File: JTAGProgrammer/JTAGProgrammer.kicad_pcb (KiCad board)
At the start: 4 copper layers, 39 x 59 mm, 111 parts, among them J1 USB_B_Micro, J2 878325623, J3 Conn_01x06, J4 Conn_01x06, J5 Conn_01x03, U1 LP2985-3.3, U2 FT2232HL, U3 93LC56B, U4 74LVC3G17, U5 74LVC3G17, U6 74LVC3G17, U7 74LVC3G17, U8 LP2985-2.5, Y1 RH100-12.000-10-3030-TR

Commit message: Add LCSC part numbers
Signed-off-by: Anthony Bernaert <anthony.bernaert@gmail.com>
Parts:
- R6: value 12K 1% -> 12K
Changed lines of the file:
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@@
     (descr "SOD-323")
     (tags "SOD-323")
+    (property "LCSC" "C324473")
     (property "Sheetfile" "JTAG.kicad_sch")
     (property "Sheetname" "JTAG")
@@
   (footprint "PGB1010603MR:DIOC1608X36N" (layer "F.Cu")
     (at 98.5 85.349455 90)
+    (property "LCSC" "C142698")
     (property "MANUFACTURER" "Littelfuse Inc.")
     (property "MAXIMUM_PACKAGE_HEIGHT" "0.36 mm")
@@
     (descr "SOD-323")
     (tags "SOD-323")
+    (property "LCSC" "C324473")
     (property "Sheetfile" "JTAG.kicad_sch")
     (property "Sheetname" "JTAG")
@@
   (footprint "PGB1010603MR:DIOC1608X36N" (layer "F.Cu")
     (at 88.3 86 90)
+    (property "LCSC" "C142698")
     (property "MANUFACTURER" "Littelfuse Inc.")
     (property "MAXIMUM_PACKAGE_HEIGHT" "0.36 mm")
@@
   (footprint "PGB1010603MR:DIOC1608X36N" (layer "F.Cu")
     (at 101.9 84.4 180)
+    (property "LCSC" "C142698")
     (property "MANUFACTURER" "Littelfuse Inc.")
     (property "MAXIMUM_PACKAGE_HEIGHT" "0.36 mm")
@@
     (descr "SOT, 6 Pin (https://www.jedec.org/sites/default/files/docs/Mo-178c.PDF variant AB), generated with kicad-footprint-generator ipc_gullwing_generator.py")
     (tags "SOT TO_SOT_SMD")
+    (property "LCSC" "C190271")
     (property "Sheetfile" "FTDI.kicad_sch")
     (property "Sheetname" "FTDI")
@@
     (descr "Through hole straight socket strip, 1x06, 2.54mm pitch, single row (from Kicad 4.0.7), script generated")
     (tags "Through hole socket strip THT 1x06 2.54mm single row")
+    (property "LCSC" "C40877")
     (property "Sheetfile" "JTAG.kicad_sch")
     (property "Sheetname" "JTAG")
@@
         (effects (font (size 0.9 0.8) (thickness 0.15)))
     )
-    (fp_text value "12K 1%" (at 0.1 0.85) (layer "F.Fab")
+    (fp_text value "12K" (at 0.1 0.85) (layer "F.Fab")
         (effects (font (size 0.5 0.5) (thickness 0.15)))
     )
@@
     (descr "VSSOP-8 3.0 x 3.0, http://www.ti.com/lit/ds/symlink/lm75b.pdf")
     (tags "VSSOP-8 3.0 x 3.0")
+    (property "LCSC" "C18213")
     (property "Sheetfile" "UART.kicad_sch")
     (property "Sheetname" "UART")
@@
     (descr "Inductor SMD 0603 (1608 Metric), square (rectangular) end terminal, IPC_7351 nominal, (Body size source: http://www.tortai-tech.com/upload/download/2011102023233369053.pdf), generated with kicad-footprint-generator")
     (tags "inductor")
+    (property "LCSC" "C107335")
     (property "Sheetfile" "Power.kicad_sch")
     (property "Sheetname" "Power")
@@
     (descr "SMD Crystal SERIES SMD3225/4 http://www.txccrystal.com/images/pdf/7m-accuracy.pdf, 3.2x2.5mm^2 package")
     (tags "SMD SMT crystal")
+    (property "LCSC" "C255903")
     (property "Sheetfile" "FTDI.kicad_sch")
     (property "Sheetname" "FTDI")
@@
     (descr "VSSOP-8 3.0 x 3.0, http://www.ti.com/lit/ds/symlink/lm75b.pdf")
     (tags "VSSOP-8 3.0 x 3.0")
+    (property "LCSC" "C18213")
     (property "Sheetfile" "UART.kicad_sch")
     (property "Sheetname" "UART")
@@
     (descr "Inductor SMD 0603 (1608 Metric), square (rectangular) end terminal, IPC_7351 nominal, (Body size source: http://www.tortai-tech.com/upload/download/2011102023233369053.pdf), generated with kicad-footprint-generator")
     (tags "inductor")
+    (property "LCSC" "C107335")
     (property "Sheetfile" "Power.kicad_sch")
     (property "Sheetname" "Power")
@@
     (descr "Through hole straight socket strip, 1x03, 2.54mm pitch, single row (from Kicad 4.0.7), script generated")
     (tags "Through hole socket strip THT 1x03 2.54mm single row")
+    (property "LCSC" "C146243")
     (property "Sheetfile" "JTAGProgrammer.kicad_sch")
     (property "Sheetname" "")
@@
   (footprint "PGB1010603MR:DIOC1608X36N" (layer "F.Cu")
     (at 101.9 82.75 180)
+    (property "LCSC" "C142698")
     (property "MANUFACTURER" "Littelfuse Inc.")
     (property "MAXIMUM_PACKAGE_HEIGHT" "0.36 mm")
@@
   (footprint "PGB1010603MR:DIOC1608X36N" (layer "F.Cu")
     (at 91.3 48.4)
+    (property "LCSC" "C142698")
     (property "MANUFACTURER" "Littelfuse Inc.")
     (property "MAXIMUM_PACKAGE_HEIGHT" "0.36 mm")
@@
     (descr "VSSOP-8 3.0 x 3.0, http://www.ti.com/lit/ds/symlink/lm75b.pdf")
     (tags "VSSOP-8 3.0 x 3.0")
+    (property "LCSC" "C18213")
     (property "Sheetfile" "JTAG.kicad_sch")
     (property "Sheetname" "JTAG")
@@
     (descr "Through hole straight socket strip, 1x06, 2.54mm pitch, single row (from Kicad 4.0.7), script generated")
     (tags "Through hole socket strip THT 1x06 2.54mm single row")
+    (property "LCSC" "C40877")
     (property "Sheetfile" "UART.kicad_sch")
     (property "Sheetname" "UART")
@@
     (descr "VSSOP-8 3.0 x 3.0, http://www.ti.com/lit/ds/symlink/lm75b.pdf")
     (tags "VSSOP-8 3.0 x 3.0")
+    (property "LCSC" "C18213")
     (property "Sheetfile" "JTAG.kicad_sch")
     (property "Sheetname" "JTAG")
@@
   (footprint "PGB1010603MR:DIOC1608X36N" (layer "F.Cu")
     (at 92.45 86 90)
+    (property "LCSC" "C142698")
     (property "MANUFACTURER" "Littelfuse Inc.")
     (property "MAXIMUM_PACKAGE_HEIGHT" "0.36 mm")
@@
   (footprint "PGB1010603MR:DIOC1608X36N" (layer "F.Cu")
     (at 101.9 87.7 180)
+    (property "LCSC" "C142698")
     (property "MANUFACTURER" "Littelfuse Inc.")
     (property "MAXIMUM_PACKAGE_HEIGHT" "0.36 mm")
@@
     (descr "LQFP, 64 Pin (https://www.analog.com/media/en/technical-documentation/data-sheets/ad7606_7606-6_7606-4.pdf), generated with kicad-footprint-generator ipc_gullwing_generator.py")
     (tags "LQFP QFP")
+    (property "LCSC" "C27882")
     (property "Sheetfile" "FTDI.kicad_sch")
     (property "Sheetname" "FTDI")
@@
     (descr "SOD-323")
     (tags "SOD-323")
+    (property "LCSC" "C324473")
     (property "Sheetfile" "JTAG.kicad_sch")
     (property "Sheetname" "JTAG")
@@
     (descr "SOD-323")
     (tags "SOD-323")
+    (property "LCSC" "C324473")
     (property "Sheetfile" "UART.kicad_sch")
     (property "Sheetname" "UART")
@@
   (footprint "PGB1010603MR:DIOC1608X36N" (layer "F.Cu")
     (at 94.5 86.050545 90)
+    (property "LCSC" "C142698")
     (property "MANUFACTURER" "Littelfuse Inc.")
     (property "MAXIMUM_PACKAGE_HEIGHT" "0.36 mm")
@@
     (descr "USB Micro-B receptacle, horizontal, SMD, 10118194, https://cdn.amphenol-icc.com/media/wysiwyg/files/drawing/10118194.pdf")
     (tags "USB Micro B horizontal SMD")
+    (property "LCSC" "C132563")
     (property "Sheetfile" "JTAGProgrammer.kicad_sch")
     (property "Sheetname" "")
@@
   (footprint "PGB1010603MR:DIOC1608X36N" (layer "F.Cu")
     (at 90.45 86 90)
+    (property "LCSC" "C142698")
     (property "MANUFACTURER" "Littelfuse Inc.")
     (property "MAXIMUM_PACKAGE_HEIGHT" "0.36 mm")
@@
     (descr "SOD-323")
     (tags "SOD-323")
+    (property "LCSC" "C324473")
     (property "Sheetfile" "UART.kicad_sch")
     (property "Sheetname" "UART")
@@
   (footprint "PGB1010603MR:DIOC1608X36N" (layer "F.Cu")
     (at 88.25 48.4 180)
+    (property "LCSC" "C142698")
     (property "MANUFACTURER" "Littelfuse Inc.")
     (property "MAXIMUM_PACKAGE_HEIGHT" "0.36 mm")
@@
     (at 93.35 93)
     (tags "878325623 ")
+    (property "LCSC" "C5197958")
     (property "Sheetfile" "JTAG.kicad_sch")
     (property "Sheetname" "JTAG")
@@
   (footprint "PGB1010603MR:DIOC1608X36N" (layer "F.Cu")
     (at 101.95 81.099455 180)
+    (property "LCSC" "C142698")
     (property "MANUFACTURER" "Littelfuse Inc.")
     (property "MAXIMUM_PACKAGE_HEIGHT" "0.36 mm")
@@
     (descr "Inductor SMD 0603 (1608 Metric), square (rectangular) end terminal, IPC_7351 nominal, (Body size source: http://www.tortai-tech.com/upload/download/2011102023233369053.pdf), generated with kicad-footprint-generator")
     (tags "inductor")
+    (property "LCSC" "C107335")
     (property "Sheetfile" "Power.kicad_sch")
     (property "Sheetname" "Power")
@@
     (descr "SOD-323")
     (tags "SOD-323")
+    (property "LCSC" "C324473")
     (property "Sheetfile" "UART.kicad_sch")
     (property "Sheetname" "UART")

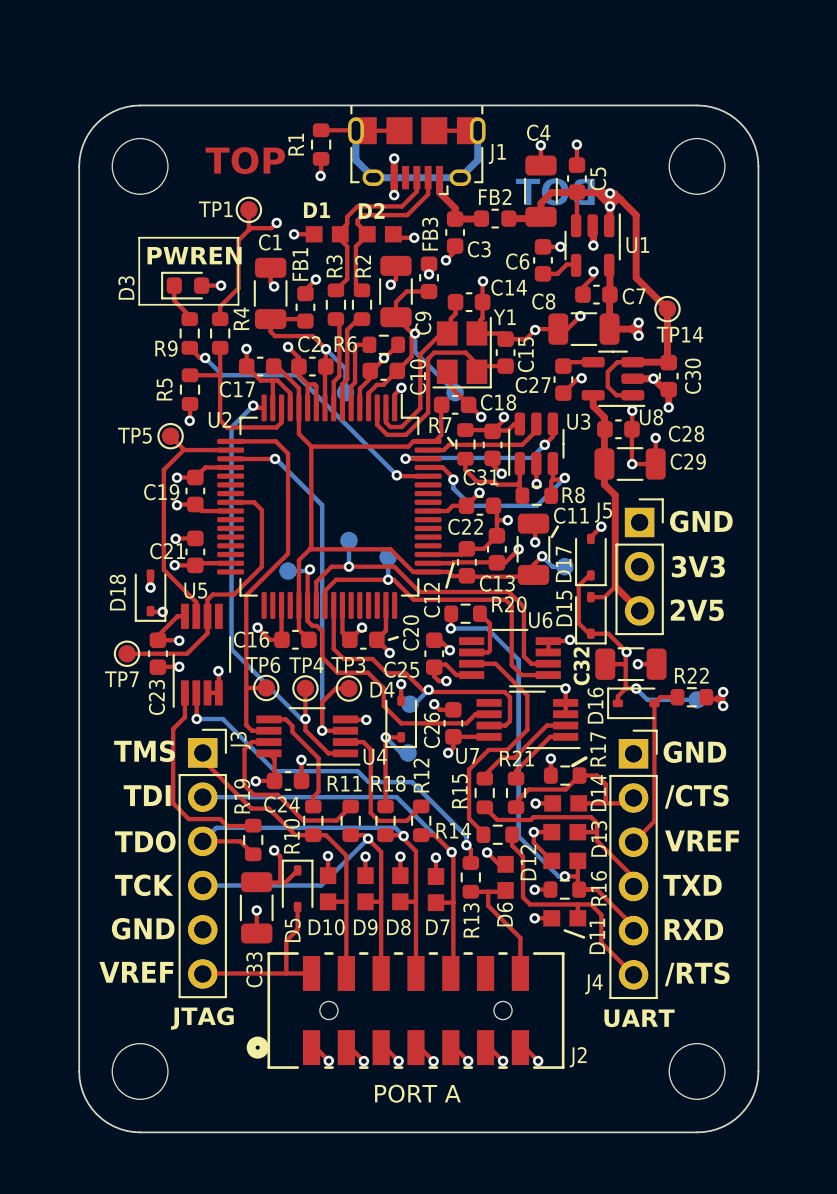
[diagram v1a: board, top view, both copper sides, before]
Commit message: Rev.2: change to USB Type-C, add VBUS fuse, VREF LED indicators
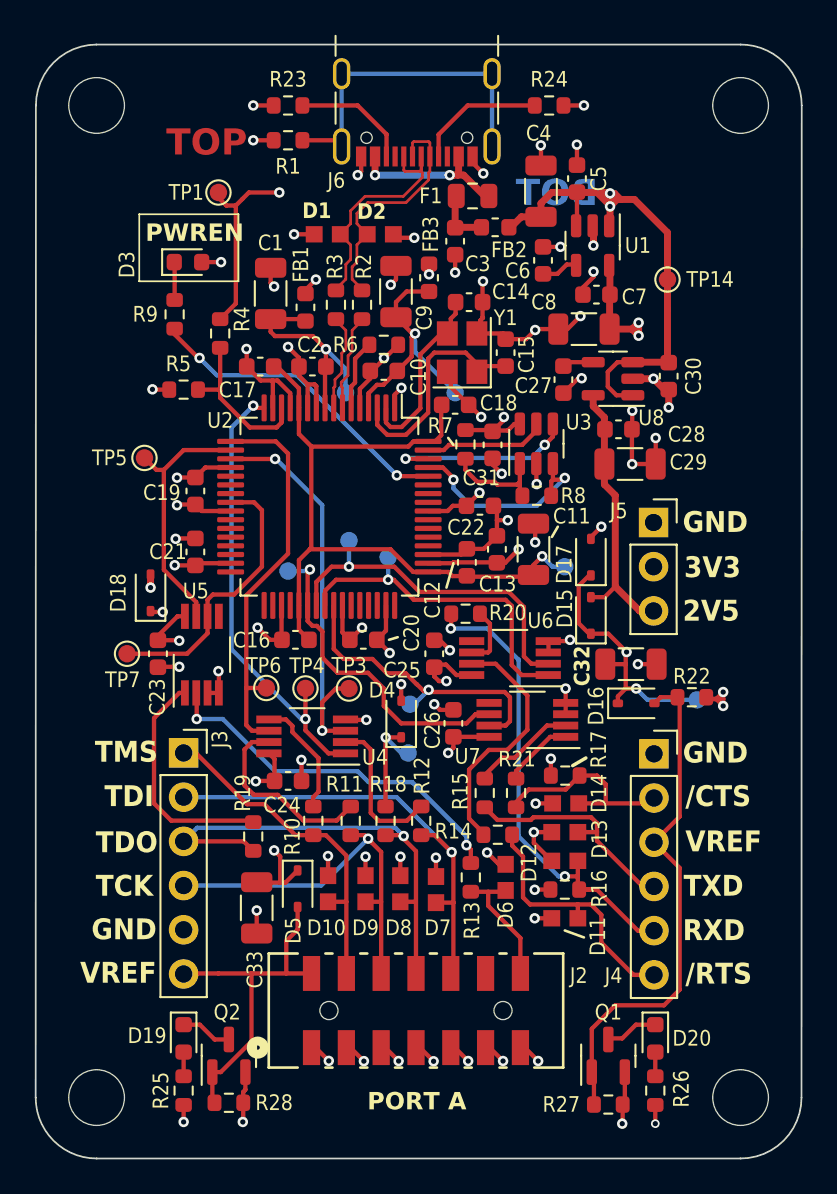
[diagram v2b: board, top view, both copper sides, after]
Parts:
- removed J1: USB_B_Micro, Connector_USB:USB_Micro-B_Amphenol_10118194_Horizontal
- added D19: LED, LED_SMD:LED_0603_1608Metric, F.Cu at (80.0, 94.6)
- added D20: LED, LED_SMD:LED_0603_1608Metric, F.Cu at (107.1, 94.6)
- added F1: 0805L075SLYR, Fuse:Fuse_0805_2012Metric, F.Cu at (96.6, 46.2)
- added J6: USB_C_Receptacle_USB2.0, Connector_USB:USB_C_Receptacle_GCT_USB4105-xx-A_16P_TopMnt_Horizontal, F.Cu at (93.4, 40.2)
- added Q1: BSS123, Package_TO_SOT_SMD:SOT-23, F.Cu at (104.4, 95.6)
- added Q2: BSS123, Package_TO_SOT_SMD:SOT-23, F.Cu at (82.6, 95.6)
- added R23: 5K1, Resistor_SMD:R_0603_1608Metric, F.Cu at (86.0, 41.0)
- added R24: 5K1, Resistor_SMD:R_0603_1608Metric, F.Cu at (101.0, 41.0)
- added R25: 100R, Resistor_SMD:R_0603_1608Metric, F.Cu at (80.0, 97.6)
- added R26: 100R, Resistor_SMD:R_0603_1608Metric, F.Cu at (107.1, 97.6)
- added R27: 10K, Resistor_SMD:R_0603_1608Metric, F.Cu at (104.4, 98.4)
- added R28: 10K, Resistor_SMD:R_0603_1608Metric, F.Cu at (82.6, 98.3)
- moved H1 4.30 mm to (75.0, 41.0)
- moved H2 4.30 mm to (112.0, 41.0)
- moved H3 2.92 mm to (75.0, 98.0)
- moved H4 2.92 mm to (112.0, 98.0)
- moved TP1 2.02 mm to (82.0, 46.0)
- moved TP5 1.95 mm to (77.8, 61.2)
- moved R1 1.92 mm to (86.0, 43.0), turned to 180 degrees
- moved TP14 1.70 mm to (107.8, 51.0)
- moved R9 1.40 mm to (79.5, 53.0)
- moved D3 1.35 mm to (80.2, 50.0)
- moved J4 1.18 mm to (107.0, 78.2)
- moved J3 1.10 mm to (80.0, 78.2)
- moved J5 0.80 mm to (107.0, 65.0)
- moved C3 0.50 mm to (95.6, 48.8)
- moved FB2 0.50 mm to (97.9, 48.0)
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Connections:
- net /FTDI/USB_DM renamed /USB_D-
- net /FTDI/USB_DP renamed /USB_D+
- net /Power/VBUS renamed Net-(C3-Pad1)
- net Net-(U2-DM) renamed /FTDI/FTDI_D-
- net Net-(U2-DP) renamed /FTDI/FTDI_D+
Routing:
- net /UART/VREF_CONN: track 9.95 -> 29.9 mm
- net /JTAG/VREF: track 10.3 -> 20.1 mm
- net /Power/VBUS: track 0.00 -> 9.30 mm, vias 0 -> 2
- net GND: track 112.6 -> 121.3 mm, vias 61 -> 65
- net Net-(J6-CC1): track 0.00 -> 7.48 mm
- net Net-(J6-CC2): track 0.00 -> 6.80 mm
- net /USB_D+: track 9.92 -> 14.2 mm
- net /USB_D-: track 10.2 -> 14.2 mm
- net /VBUS_FILT: track 42.2 -> 45.5 mm
- net Net-(D20-K): track 0.00 -> 3.05 mm
- net Net-(D19-K): track 0.00 -> 2.95 mm
- net /USB_SHIELD: track 17.0 -> 19.4 mm
- net /JTAG/TDO_CONN: track 24.7 -> 26.8 mm
- net +3V3: track 33.1 -> 35.1 mm, vias 13 -> 15
- net Net-(R19-Pad1): track 11.7 -> 13.4 mm
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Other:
- board size 39 x 59 mm -> 44 x 64 mm
- board text added: "FTDI JTAG programmer © 2025 A. Bernaert"
- board text removed: "FTDI JTAG programmer © 2024 A. Bernaert"
- board text removed: "JTAG"
- board text removed: "UART"
